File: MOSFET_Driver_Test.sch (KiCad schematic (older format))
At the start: 20 parts, among them Q10 TPHR8504PL, Q11 TPHR8504PL, Q12 TPHR8504PL, Q7 TPHR8504PL, Q8 TPHR8504PL, Q9 TPHR8504PL, U1 FD6288Q

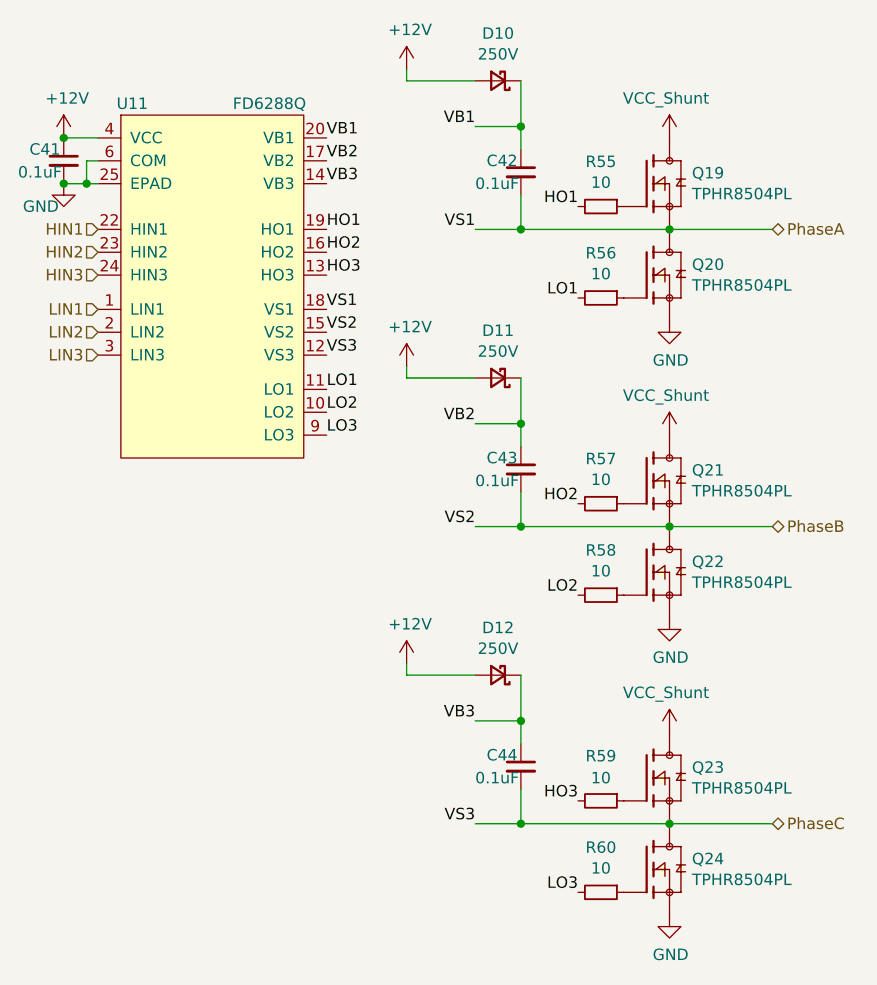
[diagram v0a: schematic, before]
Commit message: Added a test circuit to figure out best configuration
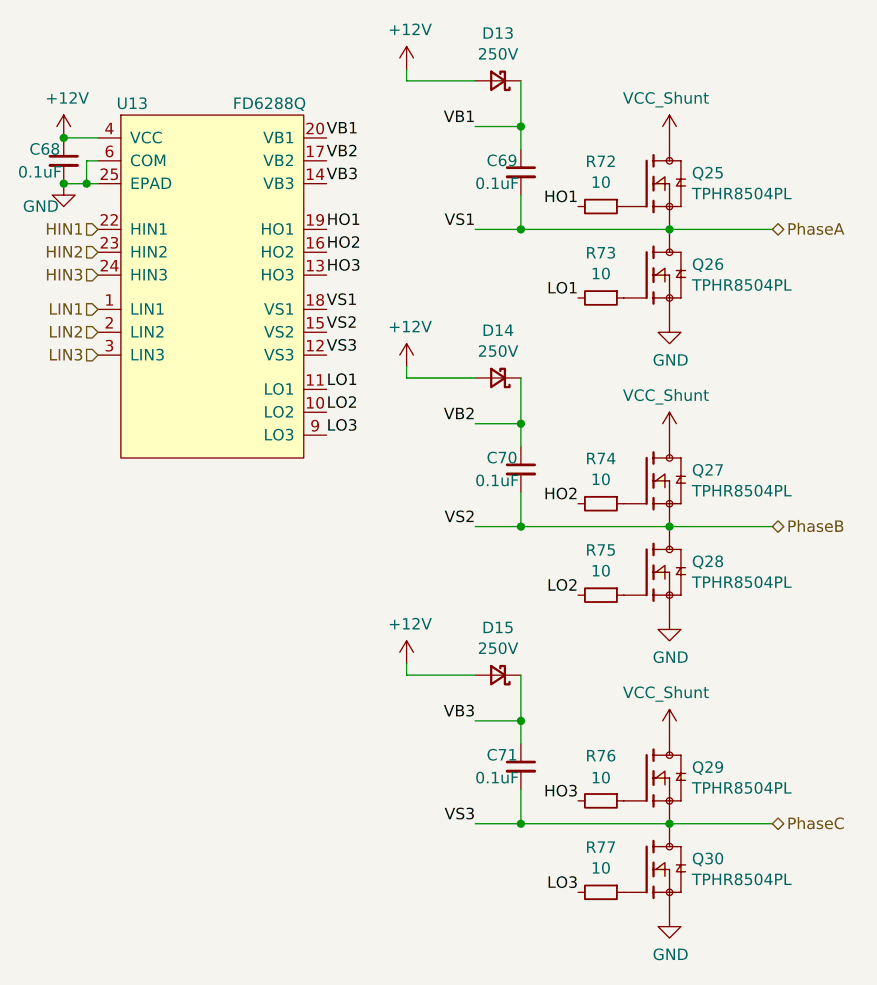
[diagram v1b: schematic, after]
